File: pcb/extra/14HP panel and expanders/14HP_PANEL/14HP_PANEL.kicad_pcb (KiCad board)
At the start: 2 copper layers, 71.1 x 128.5 mm, 11 parts

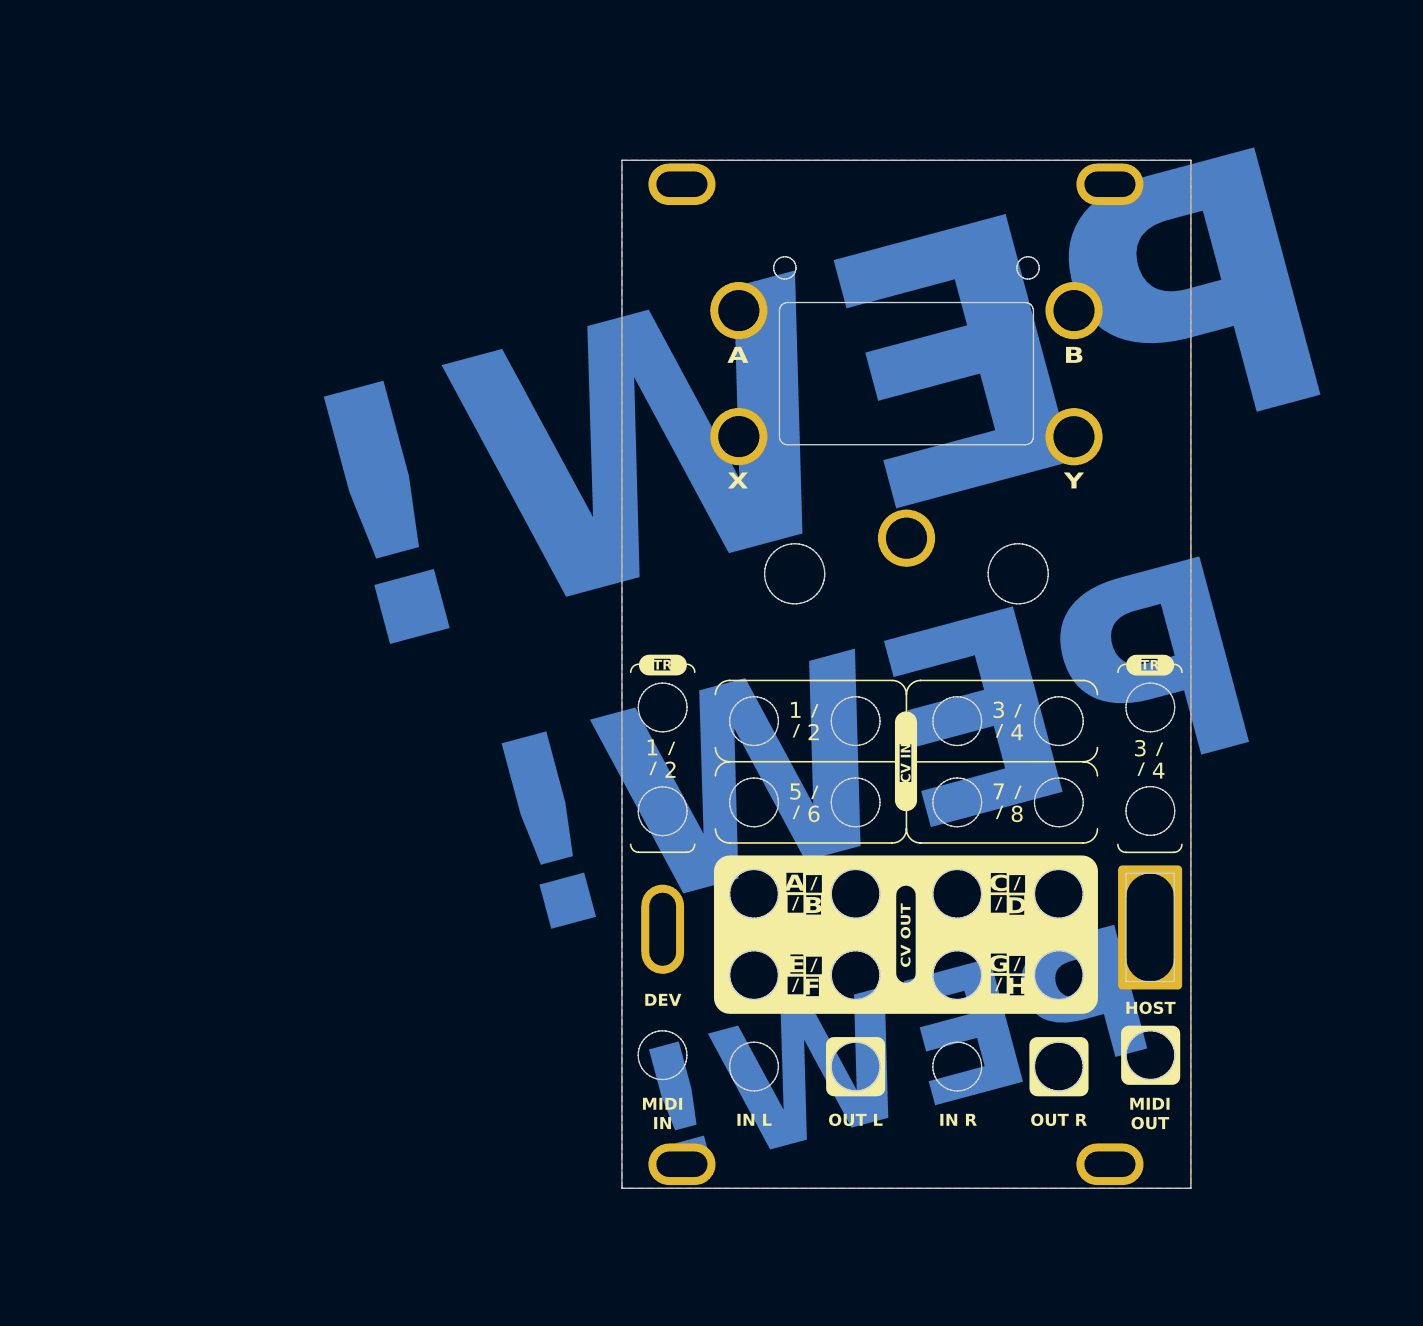
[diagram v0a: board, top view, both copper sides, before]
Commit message: fixed 14 panel copper layer overhang, generated gerber files, and created BOM for expansion panels
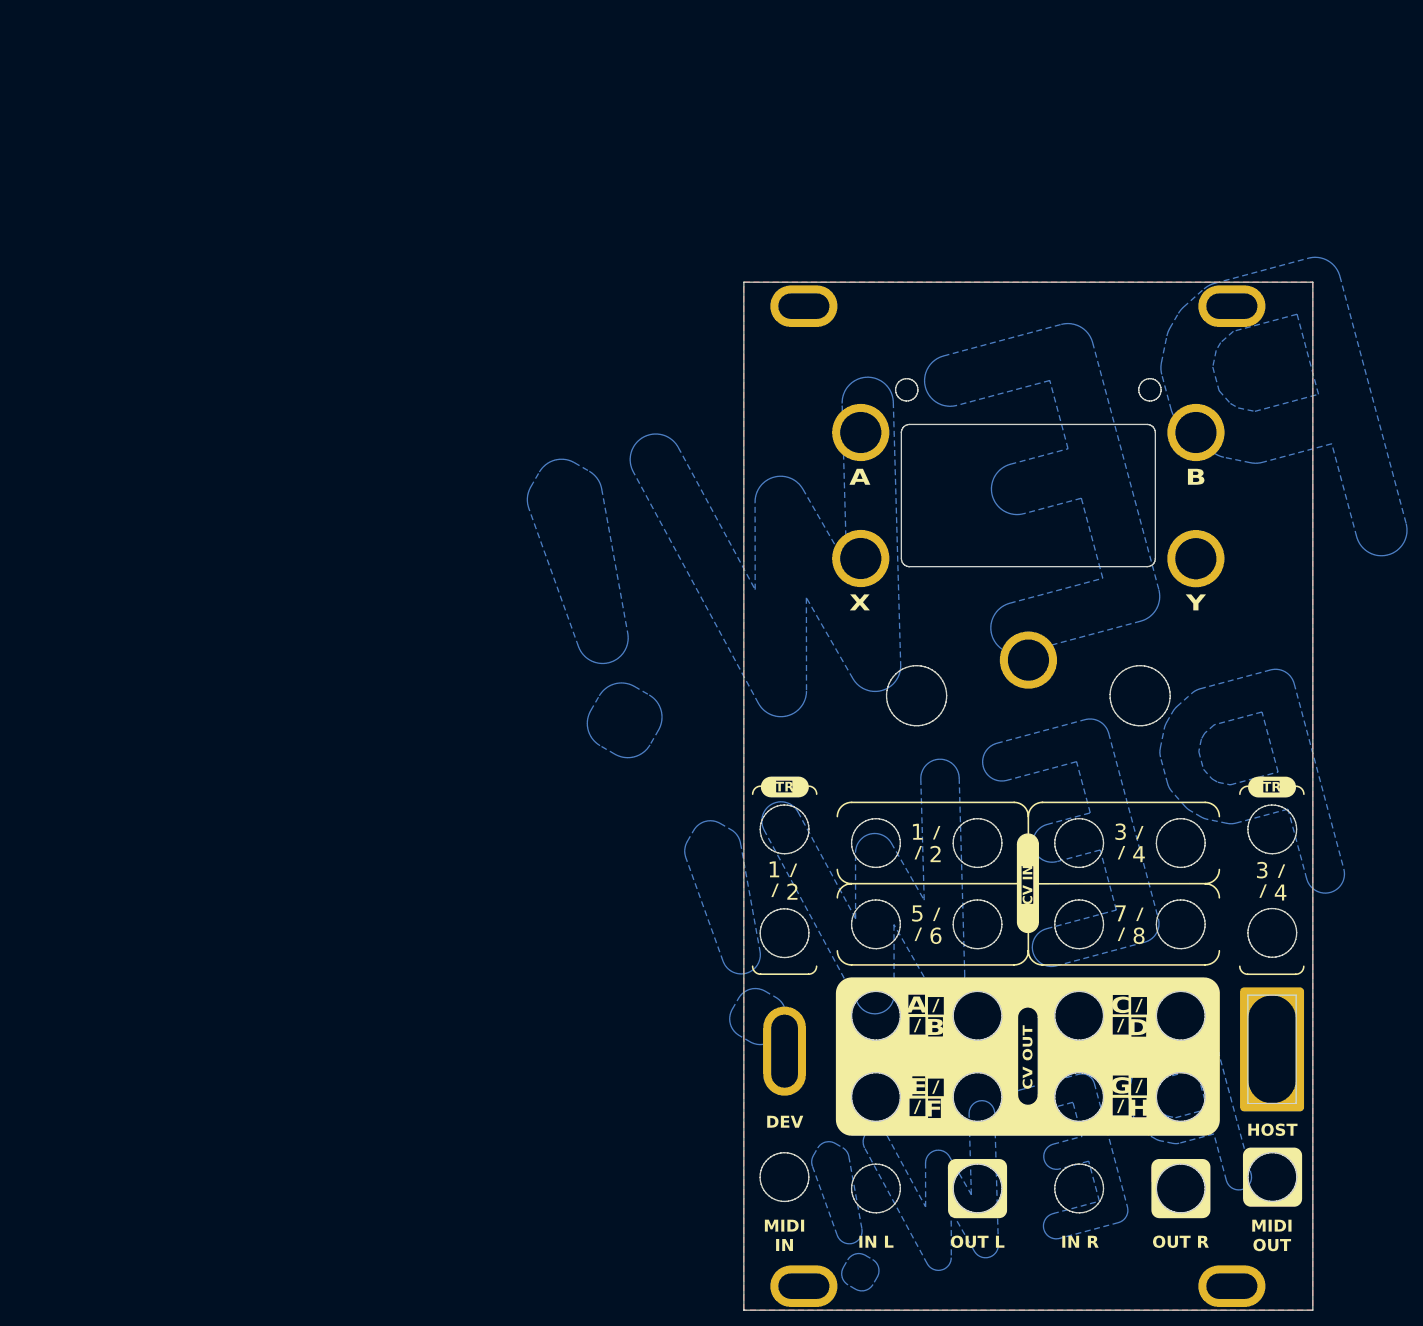
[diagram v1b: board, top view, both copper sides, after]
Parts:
- moved REF** 21.6 mm to (97.2, 59.4)
- moved REF** 21.6 mm to (45.7, 136.8)
- moved REF** 21.6 mm to (55.2, 75.2)
- moved REF** 21.6 mm to (48.1, 43.6)
- moved REF** 21.6 mm to (55.2, 59.4)
- moved REF** 21.6 mm to (106.7, 136.5)
- moved REF** 21.6 mm to (101.6, 43.6)
- moved REF** 21.6 mm to (97.1, 75.2)
- moved REF** 21.6 mm to (76.2, 87.9)
- moved REF** 21.6 mm to (48.1, 166.1)
- moved REF** 21.6 mm to (101.6, 166.1)
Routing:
- added copper zone on B.Cu, net (none)
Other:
- board text removed: "PEW!"
